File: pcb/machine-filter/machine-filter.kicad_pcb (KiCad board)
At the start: 2 copper layers, 150 x 107 mm, 162 parts, among them J1 PJ398SM, J10 PJ398SM, J11 PJ398SM, J12 PJ398SM, J13 EURO PWR 2x5, J14 EXPANSION 2x4, J15 TF-01A, J2 PJ398SM, J3 PJ398SM, J4 PJ398SM, J5 PJ398SM, J6 PJ398SM, J7 PJ398SM, J8 PJ398SM, J9 PJ398SM, U1 LMV324, U2 LMV324, U3 TL072, U4 TL072, U5 LM4040-10, U6 74HC4051, U7 LM324, U8 LM324

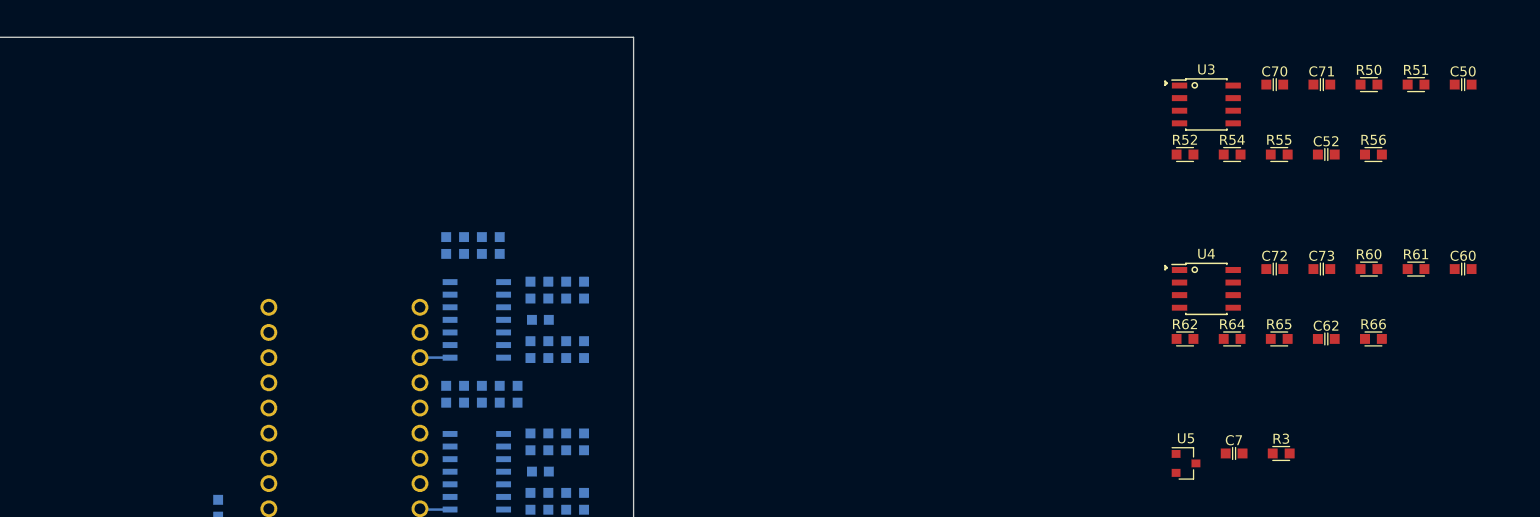
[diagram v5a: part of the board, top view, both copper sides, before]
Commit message: Placement step 5: U3 and U4 with their groups; codec traces Seed3 16 -> R52, 18 -> R60
DRC: no shorts or clearance problems (silkscreen overlaps only). konnect_place.py
now flips before rotating, so steps are repeatable. Workflow notes: d's scope rule
(no passive fine-tuning until all primaries and secondaries are placed).

Co-Authored-By: Claude Opus 5.5 <noreply@anthropic.com>
Claude-Session: https://claude.ai/code/session_01Cf5qNBi3oNHhbCjPHvswth
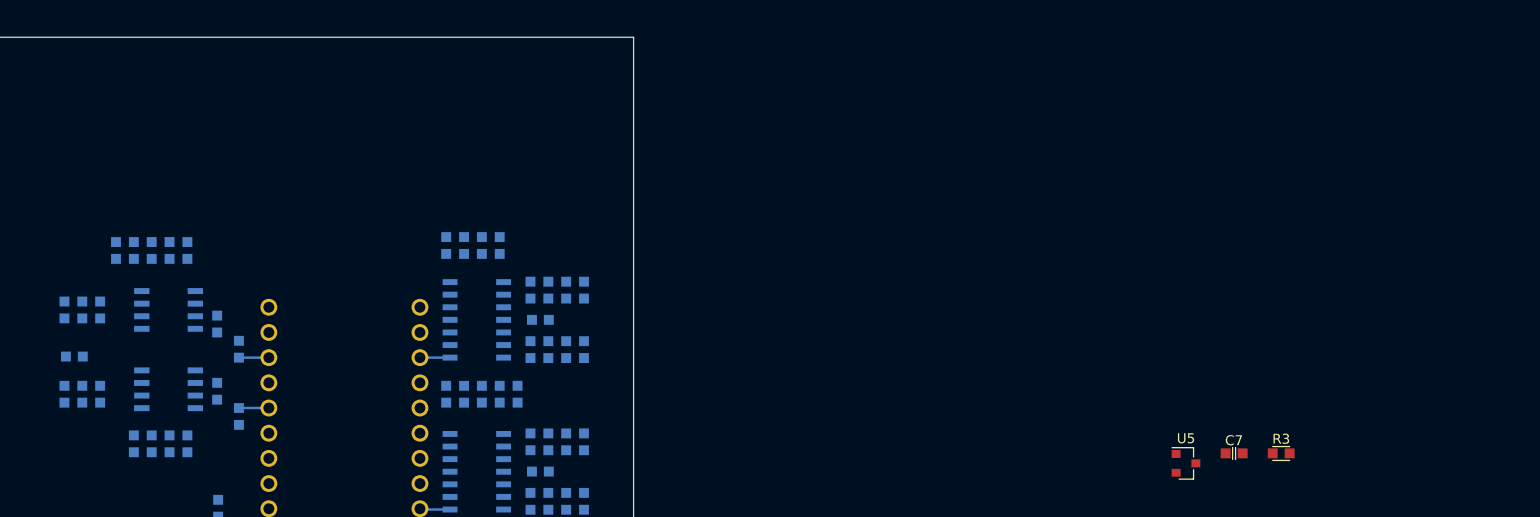
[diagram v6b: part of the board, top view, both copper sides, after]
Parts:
- C50, C52, C60, C62, C70, C71, C72, C73, R50, R51, R52, R54, R55, R56, R60, R61, R62, R64, R65, R66, U3, U4: moved to B.Cu
- moved C50 141.0 mm to (196.6, 100.0), turned to 90 degrees
- moved C60 139.3 mm to (194.8, 91.5), turned to 90 degrees
- moved R51 138.1 mm to (194.8, 100.0), turned to 90 degrees
- moved R61 136.4 mm to (193.0, 91.5), turned to 90 degrees
- moved R50 135.2 mm to (193.0, 100.0), turned to 90 degrees
- moved C71 128.8 mm to (194.0, 96.2)
- moved R66 121.7 mm to (203.6, 85.5), turned to 90 degrees
- moved C73 121.6 mm to (198.2, 85.5), turned to 90 degrees
- moved C52 120.3 mm to (203.6, 105.0), turned to 90 degrees
- moved R56 119.0 mm to (208.4, 99.7), turned to 90 degrees
- moved C62 118.8 mm to (201.8, 85.5), turned to 90 degrees
- moved R55 117.4 mm to (201.8, 105.0), turned to 90 degrees
- moved R65 115.9 mm to (200.0, 85.5), turned to 90 degrees
- moved C70 115.5 mm to (205.4, 105.0), turned to 90 degrees
- moved R54 114.5 mm to (200.0, 105.0), turned to 90 degrees
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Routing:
- net CODEC_OUT_L: track 0.00 -> 3.02 mm
- net CODEC_IN_L: track 0.00 -> 3.02 mm

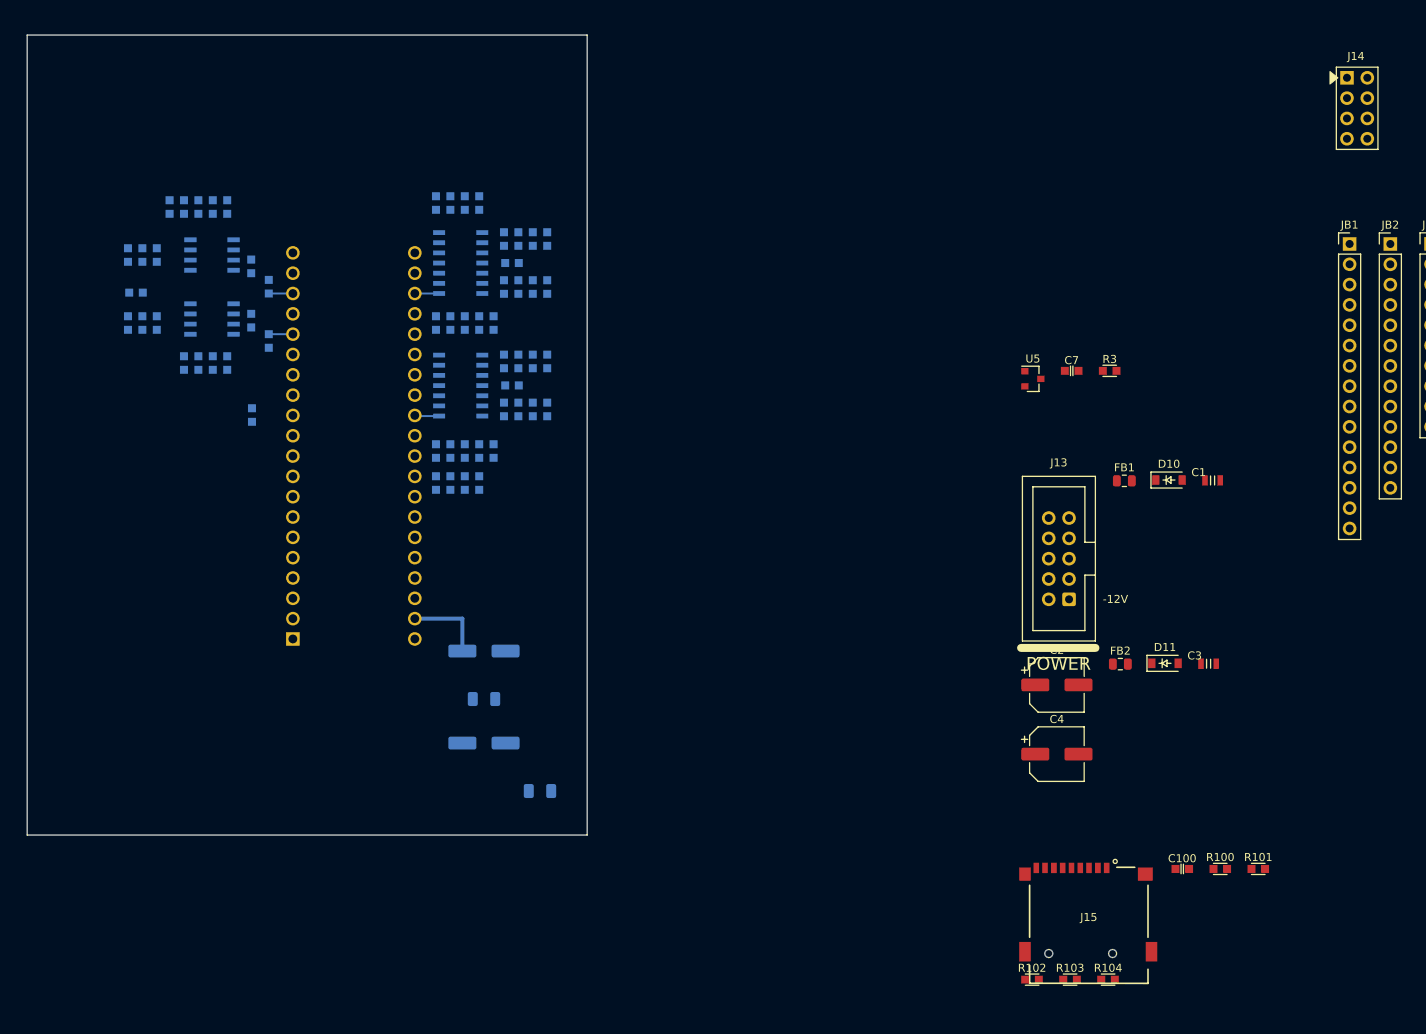
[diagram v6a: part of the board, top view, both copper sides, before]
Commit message: Placement round one (main board): U5, J13, J15, J14 as blocks; fixes; round-one picture
- pack mode in konnect_place.py (a group as one block fitted to its corner;
  back-side mirroring of the courtyard offset), common-net picking by name.
- U5's group repacked inside the board edge; trace U5 -> R28.
- J15/J14 critical traces deleted (they ran along the connector's pin row);
  flagged for d. DRC: only R70/R100 courtyard overlap (minor parts).

Co-Authored-By: Claude Opus 5.5 <noreply@anthropic.com>
Claude-Session: https://claude.ai/code/session_01Cf5qNBi3oNHhbCjPHvswth
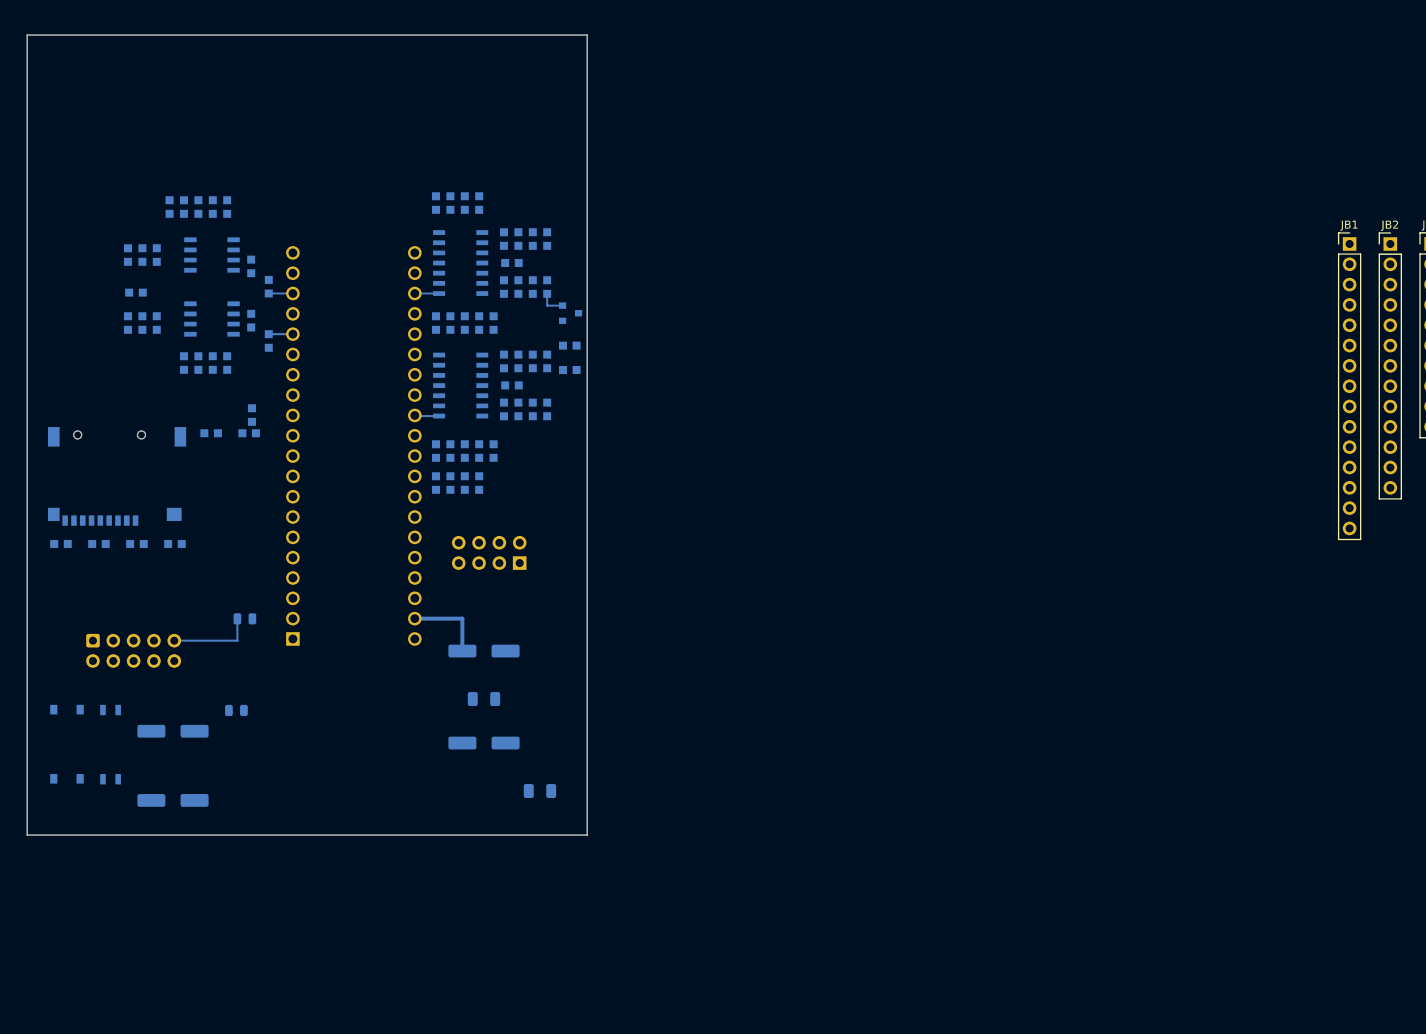
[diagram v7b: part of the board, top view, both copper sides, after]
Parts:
- C1, C100, C2, C3, C4, C7, D10, D11, FB1, FB2, J13, J14, J15, R100, R101, R102, R103, R104, R3, U5: moved to B.Cu
- moved R101 155.1 mm to (184.6, 127.6)
- moved C1 140.7 mm to (190.8, 148.4)
- moved D10 140.7 mm to (185.4, 148.3)
- moved C3 138.0 mm to (190.8, 157.0)
- moved D11 138.0 mm to (185.4, 157.0)
- moved J15 134.4 mm to (191.7, 117.5)
- moved C100 133.0 mm to (203.4, 113.8)
- moved R100 133.0 mm to (208.1, 113.8)
- moved R102 128.7 mm to (189.4, 127.6)
- moved R103 128.7 mm to (194.1, 127.6)
- moved R104 128.7 mm to (198.9, 127.6)
- moved J14 121.9 mm to (238.2, 128.7), turned to 90 degrees
- moved J13 116.2 mm to (193.7, 141.0), turned to 90 degrees
- moved FB1 111.3 mm to (207.6, 137.0)
- moved C2 110.6 mm to (198.6, 151.0)
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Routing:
- net Net-(FB1-Pad1): track 0.00 -> 10.6 mm
- net -10V_REF: track 0.00 -> 3.40 mm

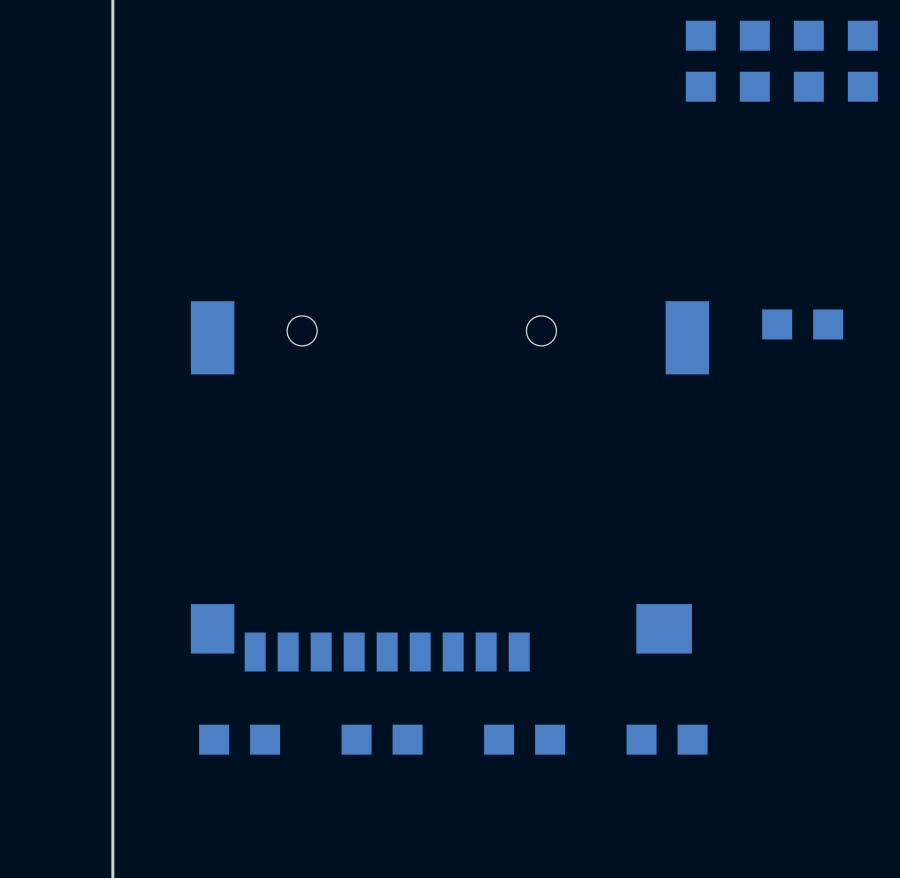
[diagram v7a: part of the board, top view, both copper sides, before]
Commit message: J15 rotated 90 deg CCW (d)
Co-Authored-By: Claude Opus 5.5 <noreply@anthropic.com>
Claude-Session: https://claude.ai/code/session_01Cf5qNBi3oNHhbCjPHvswth
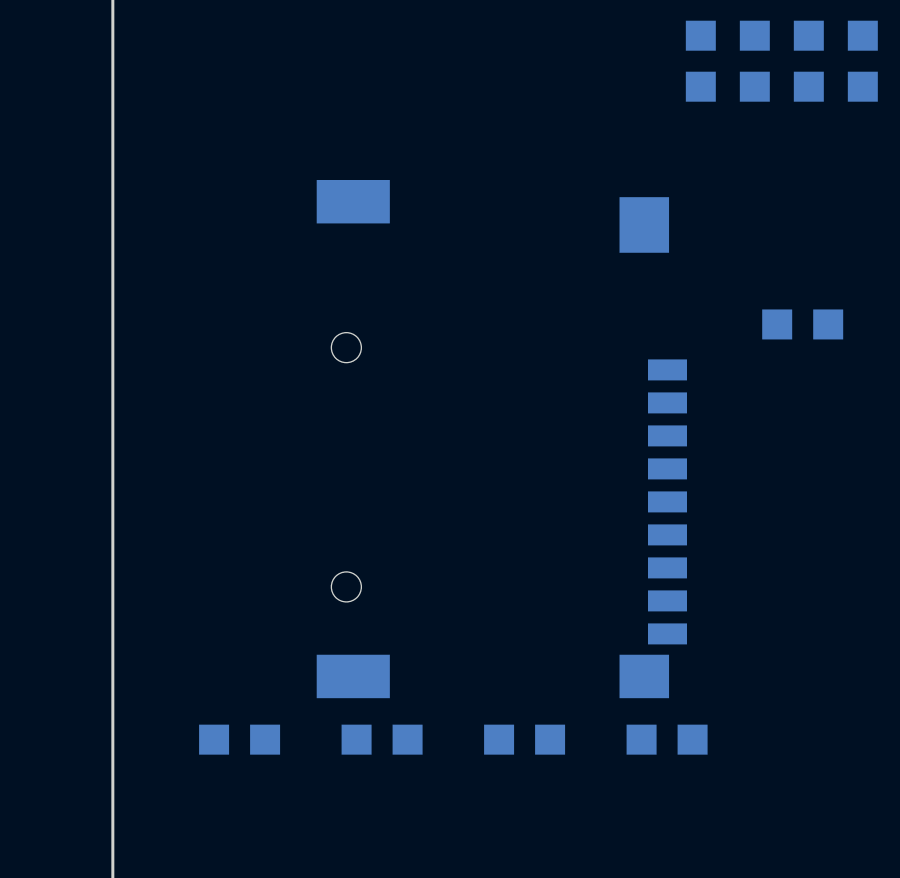
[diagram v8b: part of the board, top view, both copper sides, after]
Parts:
- turned J15 to 90 degrees
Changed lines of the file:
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@@
 	(footprint "filter-module:TF-01A"
 		(layer "B.Cu")
-		(at 191.715 117.52)
+		(at 191.715 117.52 90)
 		(descr "microSD socket, push-push, HRO TF-01A (LCSC C91145). From Electrosmith Seed3 Eurorack Dev Kit Rev3 (b4479f9), originally SnapEDA.")
 		(property "Reference" "J15"
-			(at 0 1 180)
+			(at 0 1 -90)
 			(unlocked yes)
 			(layer "B.SilkS")
@@
 		)
 		(property "Value" "TF-01A"
-			(at 0 -1 180)
+			(at 0 -1 -90)
 			(unlocked yes)
 			(layer "B.SilkS")
@@
 		)
 		(property "Datasheet" ""
-			(at 0 0 180)
+			(at 0 0 -90)
 			(layer "B.Fab")
 			(hide yes)
@@
 		)
 		(property "Description" ""
-			(at 0 0 180)
+			(at 0 0 -90)
 			(layer "B.Fab")
 			(hide yes)
@@
 		(duplicate_pad_numbers_are_jumpers no)
 		(fp_line
+			(start 7.39902 -7.2627)
+			(end 7.4 -5.5)
+			(stroke
+				(width 0.2032)
+				(type solid)
+			)
+			(layer "B.SilkS")
+		)
+		(fp_line
+			(start -7.39902 -7.25)
+			(end 7.39902 -7.2627)
+			(stroke
+				(width 0.2032)
+				(type solid)
+			)
+			(layer "B.SilkS")
+		)
+		(fp_line
 			(start -7.4 -5)
 			(end -7.39902 -7.25)
@@
 		)
 		(fp_line
+			(start 7.4 -1.5)
+			(end 7.4 5)
+			(stroke
+				(width 0.2032)
+				(type solid)
+			)
+			(layer "B.SilkS")
+		)
+		(fp_line
 			(start -7.4 5)
 			(end -7.4 -1.5)
@@
 		)
 		(fp_line
-			(start -7.39902 -7.25)
-			(end 7.39902 -7.2627)
-			(stroke
-				(width 0.2032)
-				(type solid)
-			)
-			(layer "B.SilkS")
-		)
-		(fp_line
 			(start 3.5 7.25)
 			(end 5.738 7.25)
-			(stroke
-				(width 0.2032)
-				(type solid)
-			)
-			(layer "B.SilkS")
-		)
-		(fp_line
-			(start 7.39902 -7.2627)
-			(end 7.4 -5.5)
-			(stroke
-				(width 0.2032)
-				(type solid)
-			)
-			(layer "B.SilkS")
-		)
-		(fp_line
-			(start 7.4 -1.5)
-			(end 7.4 5)
 			(stroke
 				(width 0.2032)
@@
 		)
 		(fp_line
+			(start 3.429 0.9398)
+			(end 3.429 3.302001)
+			(stroke
+				(width 0.127)
+				(type solid)
+			)
+			(layer "Dwgs.User")
+		)
+		(fp_line
 			(start -6.5278 0.9398)
 			(end 3.429 0.9398)
@@
 		)
 		(fp_line
+			(start 3.429 3.302001)
+			(end -6.5278 3.302001)
+			(stroke
+				(width 0.127)
+				(type solid)
+			)
+			(layer "Dwgs.User")
+		)
+		(fp_line
 			(start -6.5278 3.302001)
 			(end -6.5278 0.9398)
@@
 		)
 		(fp_line
-			(start 3.429 0.9398)
-			(end 3.429 3.302001)
-			(stroke
-				(width 0.127)
-				(type solid)
-			)
-			(layer "Dwgs.User")
-		)
-		(fp_line
-			(start 3.429 3.302001)
-			(end -6.5278 3.302001)
-			(stroke
-				(width 0.127)
-				(type solid)
-			)
-			(layer "Dwgs.User")
+			(start 9.36 -8.25)
+			(end -9.36 -8.25)
+			(stroke
+				(width 0.1)
+				(type solid)
+			)
+			(layer "B.Fab")
 		)
 		(fp_line
@@
 		)
 		(fp_line
+			(start 7.4 -7.25)
+			(end -7.4 -7.25)
+			(stroke
+				(width 0.2)
+				(type solid)
+			)
+			(layer "B.Fab")
+		)
+		(fp_line
+			(start -7.4 -7.25)
+			(end -7.4 7.25)
+			(stroke
+				(width 0.2)
+				(type solid)
+			)
+			(layer "B.Fab")
+		)
+		(fp_line
+			(start 7.4 7.25)
+			(end 7.4 -7.25)
+			(stroke
+				(width 0.2)
+				(type solid)
+			)
+			(layer "B.Fab")
+		)
+		(fp_line
+			(start 9.36 8.9)
+			(end 9.36 -8.25)
+			(stroke
+				(width 0.1)
+				(type solid)
+			)
+			(layer "B.Fab")
+		)
+		(fp_line
 			(start -9.36 8.9)
 			(end 9.36 8.9)
@@
 			(layer "B.Fab")
 		)
-		(fp_line
-			(start -7.4 -7.25)
-			(end -7.4 7.25)
-			(stroke
-				(width 0.2)
-				(type solid)
-			)
-			(layer "B.Fab")
-		)
-		(fp_line
-			(start 7.4 -7.25)
-			(end -7.4 -7.25)
-			(stroke
-				(width 0.2)
-				(type solid)
-			)
-			(layer "B.Fab")
-		)
-		(fp_line
-			(start 7.4 7.25)
-			(end 7.4 -7.25)
-			(stroke
-				(width 0.2)
-				(type solid)
-			)
-			(layer "B.Fab")
-		)
-		(fp_line
-			(start 9.36 -8.25)
-			(end -9.36 -8.25)
-			(stroke
-				(width 0.1)
-				(type solid)
-			)
-			(layer "B.Fab")
-		)
-		(fp_line
-			(start 9.36 8.9)
-			(end 9.36 -8.25)
-			(stroke
-				(width 0.1)
-				(type solid)
-			)
-			(layer "B.Fab")
-		)
 		(pad "1" smd rect
-			(at 2.2298 7.1738)
+			(at 2.2298 7.1738 90)
 			(size 0.7 1.3)
 			(layers "B.Cu" "B.Mask" "B.Paste")
@@
 		)
 		(pad "2" smd rect
-			(at 1.1298 7.1738)
+			(at 1.1298 7.1738 90)
 			(size 0.7 1.3)
 			(layers "B.Cu" "B.Mask" "B.Paste")
@@
 		)
 		(pad "3" smd rect
-			(at 0.0298 7.1738)
+			(at 0.0298 7.1738 90)
 			(size 0.7 1.3)
 			(layers "B.Cu" "B.Mask" "B.Paste")
@@
 		)
 		(pad "4" smd rect
-			(at -1.0702 7.1738)
+			(at -1.0702 7.1738 90)
 			(size 0.7 1.3)
 			(layers "B.Cu" "B.Mask" "B.Paste")
@@
 		)
 		(pad "5" smd rect
-			(at -2.1702 7.1738)
+			(at -2.1702 7.1738 90)
 			(size 0.7 1.3)
 			(layers "B.Cu" "B.Mask" "B.Paste")
@@
 		)
 		(pad "6" smd rect
-			(at -3.2702 7.1738)
+			(at -3.2702 7.1738 90)
 			(size 0.7 1.3)
 			(layers "B.Cu" "B.Mask" "B.Paste")
@@
 		)
 		(pad "7" smd rect
-			(at -4.3702 7.1738)
+			(at -4.3702 7.1738 90)
 			(size 0.7 1.3)
 			(layers "B.Cu" "B.Mask" "B.Paste")
@@
 		)
 		(pad "8" smd rect
-			(at -5.4702 7.1738)
+			(at -5.4702 7.1738 90)
 			(size 0.7 1.3)
 			(layers "B.Cu" "B.Mask" "B.Paste")
@@
 		)
 		(pad "CD1" smd rect
-			(at -6.5702 7.1738)
+			(at -6.5702 7.1738 90)
 			(size 0.7 1.3)
 			(layers "B.Cu" "B.Mask" "B.Paste")
@@
 		)
 		(pad "MP1" smd rect
-			(at -7.9886 6.4)
+			(at -7.9886 6.4 90)
 			(size 1.4478 1.651)
 			(layers "B.Cu" "B.Mask" "B.Paste")
@@
 		)
 		(pad "MP2" smd rect
-			(at -7.9886 -3.3)
+			(at -7.9886 -3.3 90)
 			(size 1.4478 2.4384)
 			(layers "B.Cu" "B.Mask" "B.Paste")
@@
 		)
 		(pad "MP3" smd rect
-			(at 7.8362 -3.3)
+			(at 7.8362 -3.3 90)
 			(size 1.4478 2.4384)
 			(layers "B.Cu" "B.Mask" "B.Paste")
@@
 		)
 		(pad "MP4" smd rect
-			(at 7.0612 6.4)
+			(at 7.0612 6.4 90)
 			(size 1.8542 1.651)
 			(layers "B.Cu" "B.Mask" "B.Paste")
@@
 		)
 		(pad "None" np_thru_hole circle
-			(at -5.0038 -3.5306)
+			(at -5.0038 -3.5306 90)
 			(size 0.999997 0.999997)
 			(drill 0.999997)
@@
 		)
 		(pad "None" np_thru_hole circle
-			(at 2.9718 -3.5306)
+			(at 2.9718 -3.5306 90)
 			(size 0.999997 0.999997)
 			(drill 0.999997)
